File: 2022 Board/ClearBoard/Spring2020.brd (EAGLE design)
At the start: 100 x 80 mm, 15 parts, among them U1 TB67H401FTG(O,EL)

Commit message: Lots of stuff
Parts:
- removed R18: (no value), resistor:0414/15
- added C1: ECA1CM101I, SnapEDA Library:CAPPRD250W50D500H1100
- added PWM: 68000, rcl:0204V
- added U2: ABX00012, SnapEDA Library:ARDUINO_ABX00012
- added U3: V36SE05010NRFA, SnapEDA Library:MODULE_V36SE05010NRFA
- ROSC: value (none) -> 5100; device rcl:0309/10 -> rcl:0204V
- RRS: value (none) -> 0.22; device rcl:0309/10 -> rcl:0204V
- moved RRS 59.2 mm to (54.6, 70.3), turned to 0 degrees
- moved U1 40.4 mm to (54.8, 59.0)
- moved ROSC 38.7 mm to (52.7, 65.8)
- moved GND-JUMPER 25.0 mm to (37.7, 27.3), turned to 180 degrees
- moved IMU 23.4 mm to (49.5, 19.3)
- moved U$7 20.4 mm to (27.4, 54.0)
- moved BIKE-PWR 18.1 mm to (7.36, 39.3), turned to 90 degrees
- moved C19 16.3 mm to (36.3, 42.4)
- moved RC 15.5 mm to (62.5, 37.3)
- moved U$2 11.8 mm to (22.4, 45.0)
- moved C18 11.5 mm to (18.6, 53.9), turned to 90 degrees
- moved C16 11.2 mm to (37.5, 35.4)
- moved C15 5.23 mm to (42.3, 41.4), turned to 270 degrees
- moved REAR-MOTOR 4.45 mm to (41.7, 58.0)
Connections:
- new net +5V: U2.28
- new net N$1: U3.5
- new net N$6: U2.20
- new net N$7: U2.21
- net 3.3V: now also U2.26
- net 5V: now also C1.P, U2.27, U3.7, U3.8
- net BKGND: now also U3.3
- net BKPWR: now also U3.1
- net GND: now also C1.N, U2.25, U3.4
- net IMU-CS: now also U2.16
- net MISO: now also U2.19
- net MOSI: now also U2.17
- net REAR-PWM: now also U2.11
- net REAR-PWMOUT: now also PWM.1; no longer R18.2
- net REAR-PWMR/SERVO2: now also PWM.2; no longer R18.1
- net REAR-TIMER-IN: now also U2.12
- net REVERSE: now also U2.10
- net SCK: now also U2.18
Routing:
- net BKPWR: track 19.5 -> 85.3 mm
- net 5V: track 66.8 -> 116.7 mm
- net GND: track 79.5 -> 120.4 mm, vias 0 -> 1
- net REAR-PWM: track 0.00 -> 37.7 mm
- net REAR-TIMER-IN: track 0.00 -> 36.7 mm
- net BKGND: track 96.9 -> 132.3 mm
- net 3.3V: track 54.4 -> 87.6 mm
- net MISO: track 0.00 -> 12.6 mm
- net MOSI: track 0.00 -> 11.5 mm
- net SCK: track 0.00 -> 11.1 mm
- net REVERSE: track 68.9 -> 59.5 mm
- net IMU-CS: track 0.00 -> 8.00 mm
- net REAR-PWMOUT: track 27.9 -> 22.6 mm
- net REAR-PWMR/SERVO2: track 15.2 -> 19.1 mm

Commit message: Fixed a bunch of stuff
Routed most of the board
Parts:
- removed C16: (no value), resistor:C025-050X050
- added C2, C3: (no value), resistor:C025-050X050
- added U$3: IL-711, Spring2016Optoisolator:8PINSOIC
- U$2: value IL-711 -> IL-712
- U1: device mclr:P-VQFN48-0707-0P50-004_TOS -> Test:P-VQFN48-0707-0P50-004_TOS
- moved REAR-MOTOR 39.1 mm to (2.70, 55.0), turned to 90 degrees
- moved C15 36.2 mm to (8.33, 53.9), turned to 90 degrees
- moved PWM 28.0 mm to (10.0, 48.5), turned to 0 degrees
- moved C19 25.7 mm to (13.3, 53.9), turned to 90 degrees
- moved RC 19.0 mm to (68.5, 55.3), turned to 180 degrees
- moved U$2 17.7 mm to (19.5, 62.5), turned to 180 degrees
- moved C18 9.50 mm to (28.1, 53.9)
- moved U$7 7.02 mm to (20.4, 53.5), turned to 180 degrees
- moved IMU 4.61 mm to (52.5, 22.8)
- moved BIKE-PWR 3.64 mm to (3.86, 40.3)
- moved U1 1.70 mm to (55.5, 57.5)
- moved ROSC 0.50 mm to (53.2, 65.8)
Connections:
- new net GND1: U$3.4
- new net GND2: U$3.5
- new net N$2: U1.22
- new net VDD1: U$3.1
- new net VDD2: U$3.8
- net 3.3V: now also C2.1, IMU.5; no longer IMU.4
- net 5V: now also C3.1; no longer C16.1
- net BKGND: now also C3.2; no longer C16.2, U1.22
- net CH1: now also U2.3
- net CH2: now also U2.4
- net CH3: now also U2.5
- net CH4: now also U2.6
- net GND: now also C2.2
- net REAR-PWM: now also U2.12; no longer U2.11
- net REAR-TIMER: now also U$2.6; no longer U$7.6
- net REAR-TIMER-IN: now also U$2.3, U2.10; no longer U$7.3, U2.12
- net REVERSE: now also U$2.7; no longer U$2.6, U2.10
- net REVERSE_IN: now also U$2.2, U2.11; no longer U$2.3
- net SCK: now also IMU.4; no longer IMU.5
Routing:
- net GND: track 120.4 -> 169.3 mm
- net REVERSE: track 59.5 -> 16.4 mm
- net REVERSE_IN: track 0.00 -> 35.7 mm
- net RS: track 0.00 -> 33.5 mm
- net FVCC: track 0.00 -> 20.8 mm
- net 5V: track 116.7 -> 137.0 mm
- net BKPWR: track 85.3 -> 105.5 mm
- net BKGND: track 132.3 -> 150.8 mm, vias 0 -> 2
- net REAR-PWMOUT: track 22.6 -> 10.4 mm
- net F+: track 0.00 -> 12.0 mm, vias 0 -> 2
- net REAR-PWMR/SERVO2: track 19.1 -> 8.07 mm
- net CH3: track 0.00 -> 9.56 mm
- net CH1: track 0.00 -> 8.60 mm
- net REAR-PWM: track 37.7 -> 29.3 mm
- net CH4: track 0.00 -> 7.24 mm
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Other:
- board size 100 x 80 mm -> 81 x 72 mm

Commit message: Almost done with place and route
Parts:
- removed C1: ECA1CM101I, SnapEDA Library:CAPPRD250W50D500H1100
- removed U3: V36SE05010NRFA, SnapEDA Library:MODULE_V36SE05010NRFA
- added PS1: NID100-5, SnapEDA Library:CONV_NID100-5
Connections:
- removed net BKGND: BIKE-PWR.1, C15.2, C19.2, C3.2, GND-JUMPER.2, REAR-MOTOR.1, U$2.5, U$7.5, U1.15, U3.3
- removed net N$1: U3.5
- net 5V: now also PS1.1, PS1.2, PS1.3, PS1.4; no longer C1.P, U3.7, U3.8
- net BKPWR: now also PS1.10, PS1.9; no longer U3.1
- net GND: now also BIKE-PWR.1, C15.2, C19.2, C3.2, GND-JUMPER.2, PS1.5, PS1.6, PS1.7, PS1.8, REAR-MOTOR.1, U$2.5, U$7.5, U1.15; no longer C1.N, U3.4
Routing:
- net GND: track 169.3 -> 0.00 mm, vias 1 -> 0
- net BKGND: track 150.8 -> 0.00 mm, vias 2 -> 0
- net 5V: track 137.0 -> 0.00 mm
- net BKPWR: track 105.5 -> 0.00 mm
- net 3.3V: track 84.2 -> 0.00 mm
- net REAR-TIMER-IN: track 38.5 -> 0.00 mm
- net REVERSE_IN: track 35.7 -> 0.00 mm
- net RS: track 33.5 -> 0.00 mm
- net REAR-PWM: track 29.3 -> 0.00 mm
- net FVCC: track 20.8 -> 0.00 mm
- net REVERSE: track 16.4 -> 0.00 mm
- net REAR-TIMER: track 15.7 -> 0.00 mm
- net F+: track 12.0 -> 0.00 mm, vias 2 -> 0
- net REAR-PWMOUT: track 10.4 -> 0.00 mm
- net CH3: track 9.56 -> 0.00 mm
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
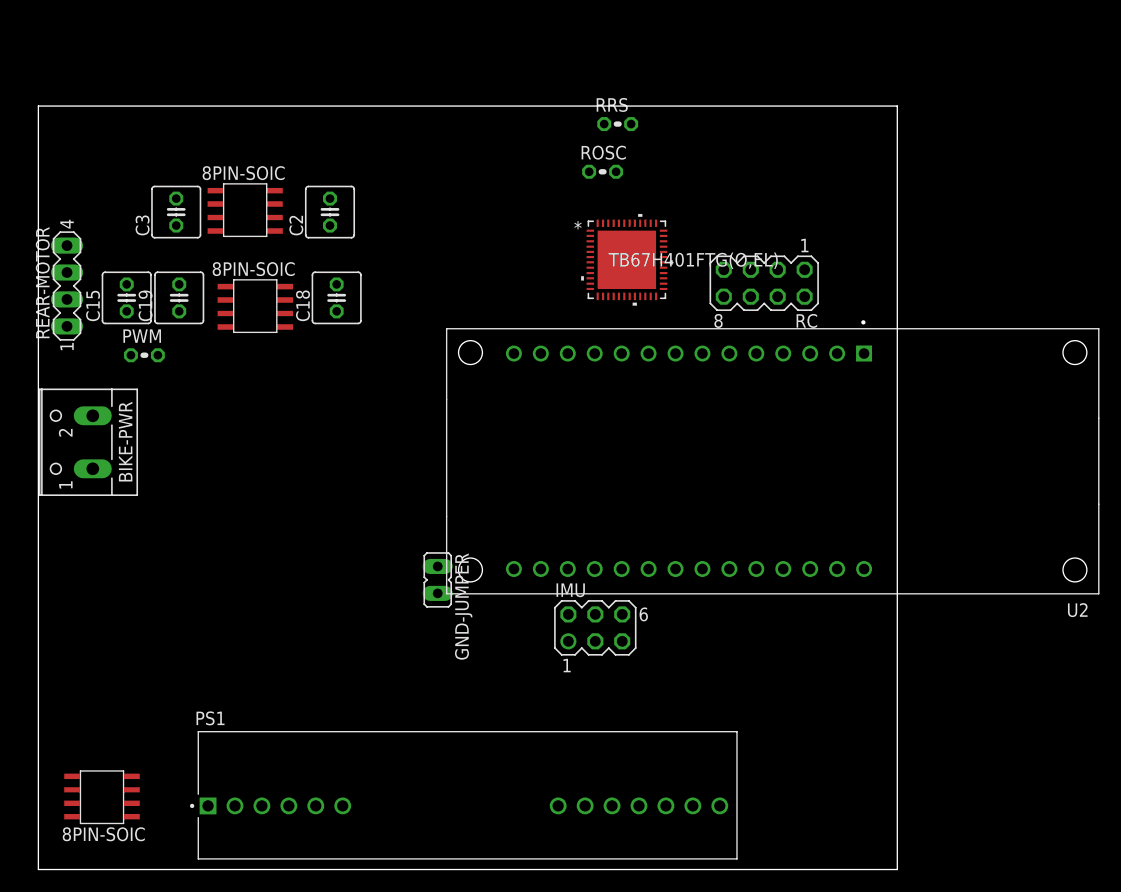
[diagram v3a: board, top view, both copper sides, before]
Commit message: Finished front motor attachments
Also positioned things in board
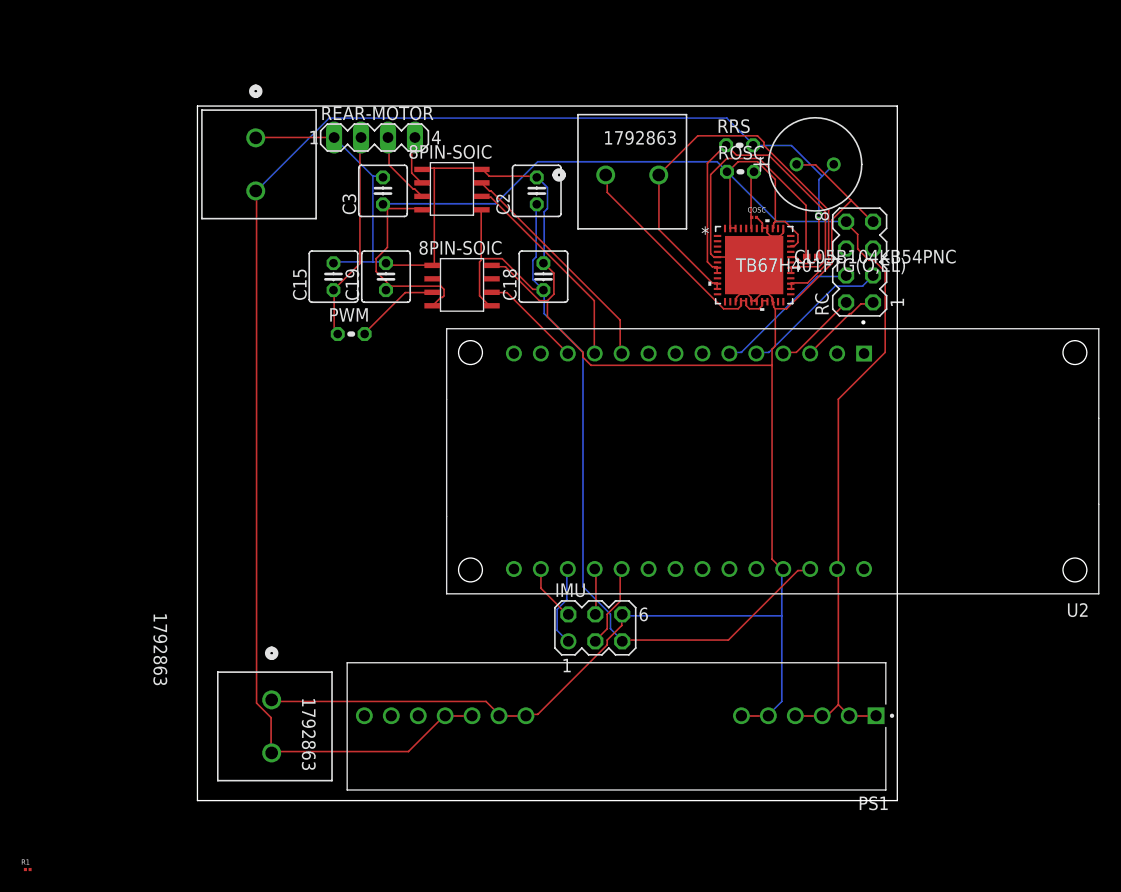
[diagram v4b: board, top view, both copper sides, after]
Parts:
- removed BIKE-PWR: (no value), con-wago-500:W237-102
- removed GND-JUMPER: (no value), jumper:JP1
- removed U$3: IL-711, Spring2016Optoisolator:8PINSOIC
- added COSC: GRM022R71A271KA01L, SnapEDA Library:CAPC0402X22N
- added CVM1: 860010674014, Test:CAP_4014_WRE
- added CVM2: CL05B104KB54PNC, Test:CAP_CL_05_SAM
- added FRT_MTR, PWR_IN, REAR_PWR: 1792863, Test:CONN_1792863_PXC
- added R1: RC0100JR-075K1L, SnapEDA Library:RESC0402X15N
- moved PS1 63.6 mm to (79.0, 14.5), turned to 180 degrees
- moved REAR-MOTOR 32.2 mm to (31.7, 69.0), turned to 0 degrees
- moved C18 19.6 mm to (47.6, 55.9)
- moved U$7 19.6 mm to (40.0, 55.5)
- moved C15 19.6 mm to (27.8, 55.9)
- moved C19 19.6 mm to (32.8, 55.9)
- moved C2 19.6 mm to (47.0, 64.0)
- moved C3 19.6 mm to (32.5, 64.0)
- moved PWM 19.6 mm to (29.5, 50.5)
- moved U$2 19.6 mm to (39.0, 64.5)
- moved ROSC 13.0 mm to (66.2, 65.8)
- moved U1 12.0 mm to (67.5, 57.0)
- moved RRS 11.7 mm to (66.1, 68.3)
- moved RC 9.22 mm to (77.5, 57.3), turned to 90 degrees
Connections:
- removed net FVCC: ROSC.1, U1.34, U1.39, U1.46, U1.47
- removed net GND1: U$3.4
- removed net GND2: U$3.5
- removed net N$2: U1.22
- removed net VDD1: U$3.1
- removed net VDD2: U$3.8
- net 5V: now also ROSC.1, U1.34, U1.39, U1.46, U1.47
- net BKPWR: now also CVM1.2, CVM2.2, PWR_IN.2, REAR_PWR.2; no longer BIKE-PWR.2
- net F+: now also FRT_MTR.2
- net F-: now also FRT_MTR.1
- net GND: now also COSC.2, CVM1.1, CVM2.1, PWR_IN.1, REAR_PWR.1, U1.22; no longer BIKE-PWR.1, GND-JUMPER.1, GND-JUMPER.2
- net N$5: now also COSC.1
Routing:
- net GND: track 0.00 -> 261.3 mm
- net 5V: track 0.00 -> 147.4 mm
- net BKPWR: track 0.00 -> 145.1 mm, vias 0 -> 1
- net 3.3V: track 0.00 -> 82.4 mm
- net F+: track 0.00 -> 44.0 mm
- net RS: track 0.00 -> 34.2 mm
- net F-: track 0.00 -> 23.2 mm
- net REAR-TIMER-IN: track 0.00 -> 21.7 mm
- net REAR-PWMOUT: track 0.00 -> 19.7 mm
- net REVERSE_IN: track 0.00 -> 19.7 mm
- net CH4: track 0.00 -> 14.1 mm
- net CH3: track 0.00 -> 14.1 mm
- net REAR-PWM: track 0.00 -> 9.57 mm
- net REAR-PWMR/SERVO2: track 0.00 -> 8.05 mm
- net CH2: track 0.00 -> 7.99 mm
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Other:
- board size 81 x 72 mm -> 66 x 65.5 mm
